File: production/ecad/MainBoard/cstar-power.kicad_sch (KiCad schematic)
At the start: 0 parts

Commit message: Update cstar-power.kicad_sch
Added the LDO
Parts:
- added C1: 22u, symbol Device:C
- added C2: 10u, symbol Device:C
- added U1: AZ1117IH-3.3TRG1, SOT223_AZ1117I_6P5X3P5_DIO, symbol 2024-02-15_17-38-45:AZ1117IH-3.3TRG1
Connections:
- new net GND: C1.2, C2.2, U1.1 (GND)
- new net P3V3: C1.1, U1.2 (OUTPUT)
- new net P5V: C2.1, U1.3 (INPUT)
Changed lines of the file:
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@@
 (kicad_sch (version 20230121) (generator eeschema)
   (paper "A4")
+  (junction (at 205.74 132.08) (diameter 0) (color 0 0 0 0)
+  )
+  (junction (at 264.16 132.08) (diameter 0) (color 0 0 0 0)
+  )
+  (wire (pts (xy 264.16 142.24) (xy 264.16 144.78))
+    (stroke (width 0) (type default))
+  )
+  (wire (pts (xy 205.74 132.08) (xy 208.28 132.08))
+    (stroke (width 0) (type default))
+  )
+  (wire (pts (xy 259.08 132.08) (xy 264.16 132.08))
+    (stroke (width 0) (type default))
+  )
+  (wire (pts (xy 264.16 134.62) (xy 264.16 132.08))
+    (stroke (width 0) (type default))
+  )
+  (wire (pts (xy 264.16 132.08) (xy 269.24 132.08))
+    (stroke (width 0) (type default))
+  )
+  (wire (pts (xy 205.74 142.24) (xy 205.74 144.78))
+    (stroke (width 0) (type default))
+  )
+  (wire (pts (xy 199.39 132.08) (xy 205.74 132.08))
+    (stroke (width 0) (type default))
+  )
+  (wire (pts (xy 233.68 146.05) (xy 233.68 148.59))
+    (stroke (width 0) (type default))
+  )
+  (wire (pts (xy 205.74 134.62) (xy 205.74 132.08))
+    (stroke (width 0) (type default))
+  )
+  (label "P3V3" (at 269.24 132.08 0) (fields_autoplaced)
+    (effects (font (size 1.27 1.27)) (justify left bottom))
+  )
+  (label "P5V" (at 199.39 132.08 0) (fields_autoplaced)
+    (effects (font (size 1.27 1.27)) (justify left bottom))
+  )
+  (symbol (lib_id "Device:C") (at 205.74 138.43 0) (unit 1)
+    (in_bom yes) (on_board yes) (dnp no) (fields_autoplaced)
+    (property "Reference" "C2" (at 209.55 137.16 0)
+      (effects (font (size 1.27 1.27)) (justify left))
+    )
+    (property "Value" "10u" (at 209.55 139.7 0)
+      (effects (font (size 1.27 1.27)) (justify left))
+    )
+    (property "Footprint" "" (at 206.7052 142.24 0)
+      (effects (font (size 1.27 1.27)) hide)
+    )
+    (property "Datasheet" "~" (at 205.74 138.43 0)
+      (effects (font (size 1.27 1.27)) hide)
+    )
+    (pin "1")
+    (pin "2")
+    (instances
+      (project "cstar-power"
+        (path "/7edd775e-47a6-46f9-8e16-808bdf3a0e15"
+          (reference "C2") (unit 1)
+        )
+      )
+    )
+  )
+  (symbol (lib_id "Device:C") (at 264.16 138.43 0) (unit 1)
+    (in_bom yes) (on_board yes) (dnp no) (fields_autoplaced)
+    (property "Reference" "C1" (at 267.97 137.16 0)
+      (effects (font (size 1.27 1.27)) (justify left))
+    )
+    (property "Value" "22u" (at 267.97 139.7 0)
+      (effects (font (size 1.27 1.27)) (justify left))
+    )
+    (property "Footprint" "" (at 265.1252 142.24 0)
+      (effects (font (size 1.27 1.27)) hide)
+    )
+    (property "Datasheet" "~" (at 264.16 138.43 0)
+      (effects (font (size 1.27 1.27)) hide)
+    )
+    (pin "1")
+    (pin "2")
+    (instances
+      (project "cstar-power"
+        (path "/7edd775e-47a6-46f9-8e16-808bdf3a0e15"
+          (reference "C1") (unit 1)
+        )
+      )
+    )
+  )
+  (symbol (lib_id "2024-02-15_17-38-45:AZ1117IH-3.3TRG1") (at 208.28 130.81 0) (unit 1)
+    (in_bom yes) (on_board yes) (dnp no) (fields_autoplaced)
+    (property "Reference" "U1" (at 233.68 120.65 0)
+      (effects (font (size 1.524 1.524)))
+    )
+    (property "Value" "AZ1117IH-3.3TRG1" (at 233.68 123.19 0)
+      (effects (font (size 1.524 1.524)))
+    )
+    (property "Footprint" "SOT223_AZ1117I_6P5X3P5_DIO" (at 204.47 111.76 0)
+      (effects (font (size 1.27 1.27) italic) hide)
+    )
+    (property "Datasheet" "AZ1117IH-3.3TRG1" (at 199.39 114.3 0)
+      (effects (font (size 1.27 1.27) italic) hide)
+    )
+    (pin "3")
+    (pin "1")
+    (pin "2")
+    (instances
+      (project "cstar-power"
+        (path "/7edd775e-47a6-46f9-8e16-808bdf3a0e15"
+          (reference "U1") (unit 1)
+        )
+      )
+    )
+  )
+  (symbol (lib_id "power:GND") (at 205.74 144.78 0) (unit 1)
+    (in_bom yes) (on_board yes) (dnp no) (fields_autoplaced)
+    (property "Reference" "#PWR02" (at 205.74 151.13 0)
+      (effects (font (size 1.27 1.27)) hide)
+    )
+    (property "Value" "GND" (at 205.74 149.86 0)
+      (effects (font (size 1.27 1.27)))
+    )
+    (property "Footprint" "" (at 205.74 144.78 0)
+      (effects (font (size 1.27 1.27)) hide)
+    )
+    (property "Datasheet" "" (at 205.74 144.78 0)
+      (effects (font (size 1.27 1.27)) hide)
+    )
+    (pin "1")
+    (instances
+      (project "cstar-power"
+        (path "/7edd775e-47a6-46f9-8e16-808bdf3a0e15"
+          (reference "#PWR02") (unit 1)
+        )
+      )
+    )
+  )
+  (symbol (lib_id "power:GND") (at 233.68 148.59 0) (unit 1)
+    (in_bom yes) (on_board yes) (dnp no) (fields_autoplaced)
+    (property "Reference" "#PWR03" (at 233.68 154.94 0)
+      (effects (font (size 1.27 1.27)) hide)
+    )
+    (property "Value" "GND" (at 233.68 153.67 0)
+      (effects (font (size 1.27 1.27)))
+    )
+    (property "Footprint" "" (at 233.68 148.59 0)
+      (effects (font (size 1.27 1.27)) hide)
+    )
+    (property "Datasheet" "" (at 233.68 148.59 0)
+      (effects (font (size 1.27 1.27)) hide)
+    )
+    (pin "1")
+    (instances
+      (project "cstar-power"
+        (path "/7edd775e-47a6-46f9-8e16-808bdf3a0e15"
+          (reference "#PWR03") (unit 1)
+        )
+      )
+    )
+  )
+  (symbol (lib_id "power:GND") (at 264.16 144.78 0) (unit 1)
+    (in_bom yes) (on_board yes) (dnp no) (fields_autoplaced)
+    (property "Reference" "#PWR01" (at 264.16 151.13 0)
+      (effects (font (size 1.27 1.27)) hide)
+    )
+    (property "Value" "GND" (at 264.16 149.86 0)
+      (effects (font (size 1.27 1.27)))
+    )
+    (property "Footprint" "" (at 264.16 144.78 0)
+      (effects (font (size 1.27 1.27)) hide)
+    )
+    (property "Datasheet" "" (at 264.16 144.78 0)
+      (effects (font (size 1.27 1.27)) hide)
+    )
+    (pin "1")
+    (instances
+      (project "cstar-power"
+        (path "/7edd775e-47a6-46f9-8e16-808bdf3a0e15"
+          (reference "#PWR01") (unit 1)
+        )
+      )
+    )
+  )
+  (sheet_instances
+    (path "/" (page "1"))
+  )
 )

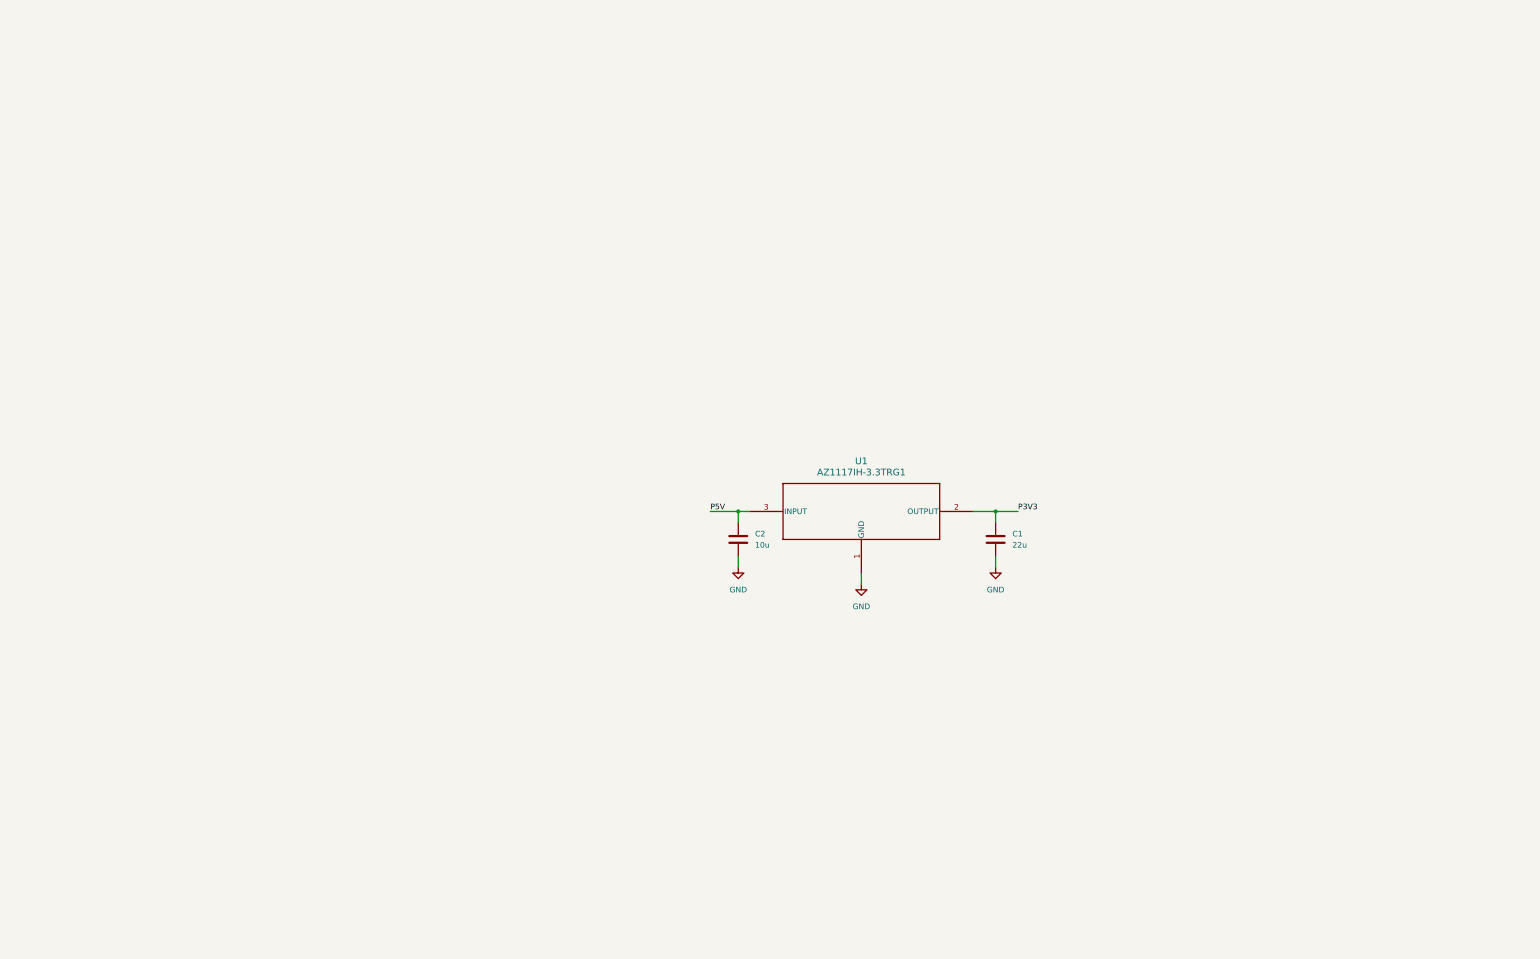
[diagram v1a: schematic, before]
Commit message: Added buck parts to the schematic, in need of more protection circuitry
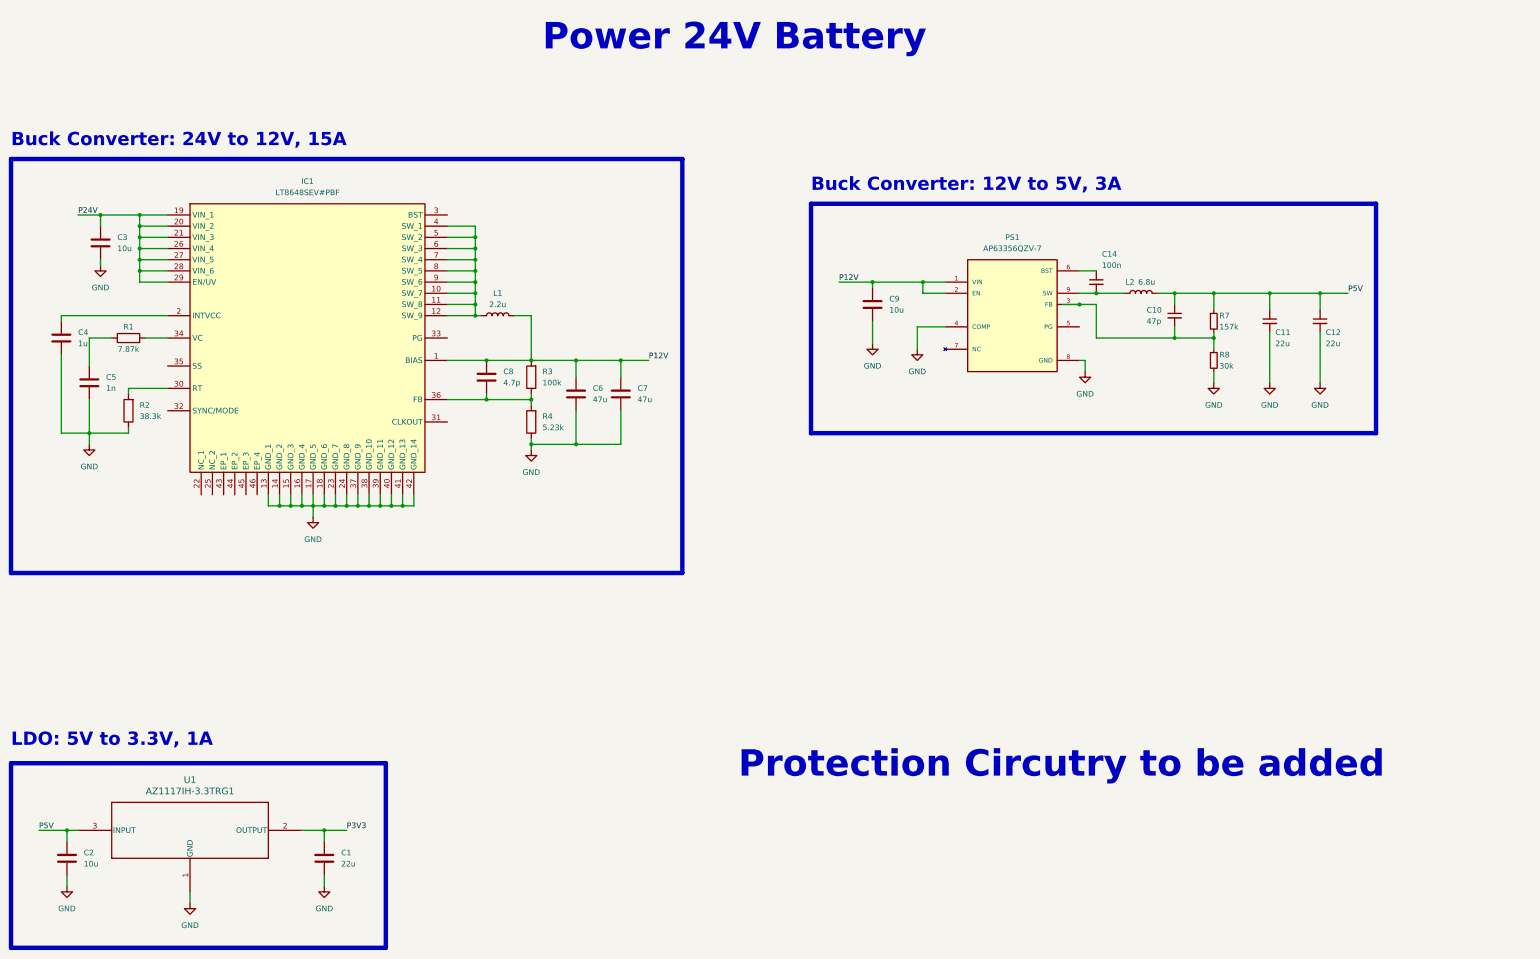
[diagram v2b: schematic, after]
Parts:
- added C10: 47p, symbol Device:C_Small
- added C11, C12: 22u, symbol Device:C_Small
- added C14: 100n, symbol Device:C_Small
- added C3, C9: 10u, symbol Device:C
- added C4: 1u, symbol Device:C
- added C5: 1n, symbol Device:C
- added C6, C7: 47u, symbol Device:C
- added C8: 4.7p, symbol Device:C
- added IC1: LT8648SEV#PBF, LT8648SEVPBF, symbol LT8648SEV#PBF:LT8648SEV#PBF
- added L1: 2.2u, symbol Device:L
- added L2: 6.8u, symbol Device:L
- added PS1: AP63356QZV-7, AP63356QZV-7:CONV_AP63356QZV-7, symbol AP63356QZV-7:AP63356QZV-7
- added R1: 7.87k, symbol Device:R
- added R2: 38.3k, symbol Device:R
- added R3: 100k, symbol Device:R
- added R4: 5.23k, symbol Device:R
- added R7: 157k, symbol Device:R_Small
- added R8: 30k, symbol Device:R_Small
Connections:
- net GND: now also C11.2, C12.2, C3.2, C4.2, C5.2, C6.2, C7.2, C9.2, IC1.13 (GND_1), IC1.14 (GND_2), IC1.15 (GND_3), IC1.16 (GND_4), IC1.17 (GND_5), IC1.18 (GND_6), IC1.23 (GND_7), IC1.24 (GND_8), IC1.37 (GND_9), IC1.38 (GND_10), IC1.39 (GND_11), IC1.40 (GND_12), IC1.41 (GND_13), IC1.42 (GND_14), PS1.4 (COMP), PS1.8 (GND), R2.1, R4.1, R8.2
- net P5V: now also C10.1, C11.1, C12.1, L2.2, R7.1
- new net: C8.2, IC1.36 (FB), R3.1, R4.2
- new net: C14.1, PS1.6 (BST)
- new net: C14.2, L2.1, PS1.9 (SW)
- new net: C5.1, R1.1
- new net: IC1.34 (VC), R1.2
- new net: C10.2, PS1.3 (FB), R7.2, R8.1
- new net: IC1.10 (SW_7), IC1.11 (SW_8), IC1.12 (SW_9), IC1.4 (SW_1), IC1.5 (SW_2), IC1.6 (SW_3), IC1.7 (SW_4), IC1.8 (SW_5), IC1.9 (SW_6), L1.1
- new net: C4.1, IC1.2 (INTVCC)
- new net: IC1.30 (RT), R2.2
- new net P12V: C6.1, C7.1, C8.1, C9.1, IC1.1 (BIAS), L1.2, PS1.1 (VIN), PS1.2 (EN), R3.2
- new net P24V: C3.1, IC1.19 (VIN_1), IC1.20 (VIN_2), IC1.21 (VIN_3), IC1.26 (VIN_4), IC1.27 (VIN_5), IC1.28 (VIN_6), IC1.29 (EN/UV)
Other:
- note added: "Buck Converter: 12V to 5V, 3A"
- note added: "Buck Converter: 24V to 12V, 15A"
- note added: "LDO: 5V to 3.3V, 1A"
- note added: "Power 24V Battery"
- note added: "Protection Circutry to be added"
- moved on the sheet: C1, C2, U1
